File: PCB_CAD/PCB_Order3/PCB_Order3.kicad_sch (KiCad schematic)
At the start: 84 parts, among them SW1 SLW-883935-2A-D

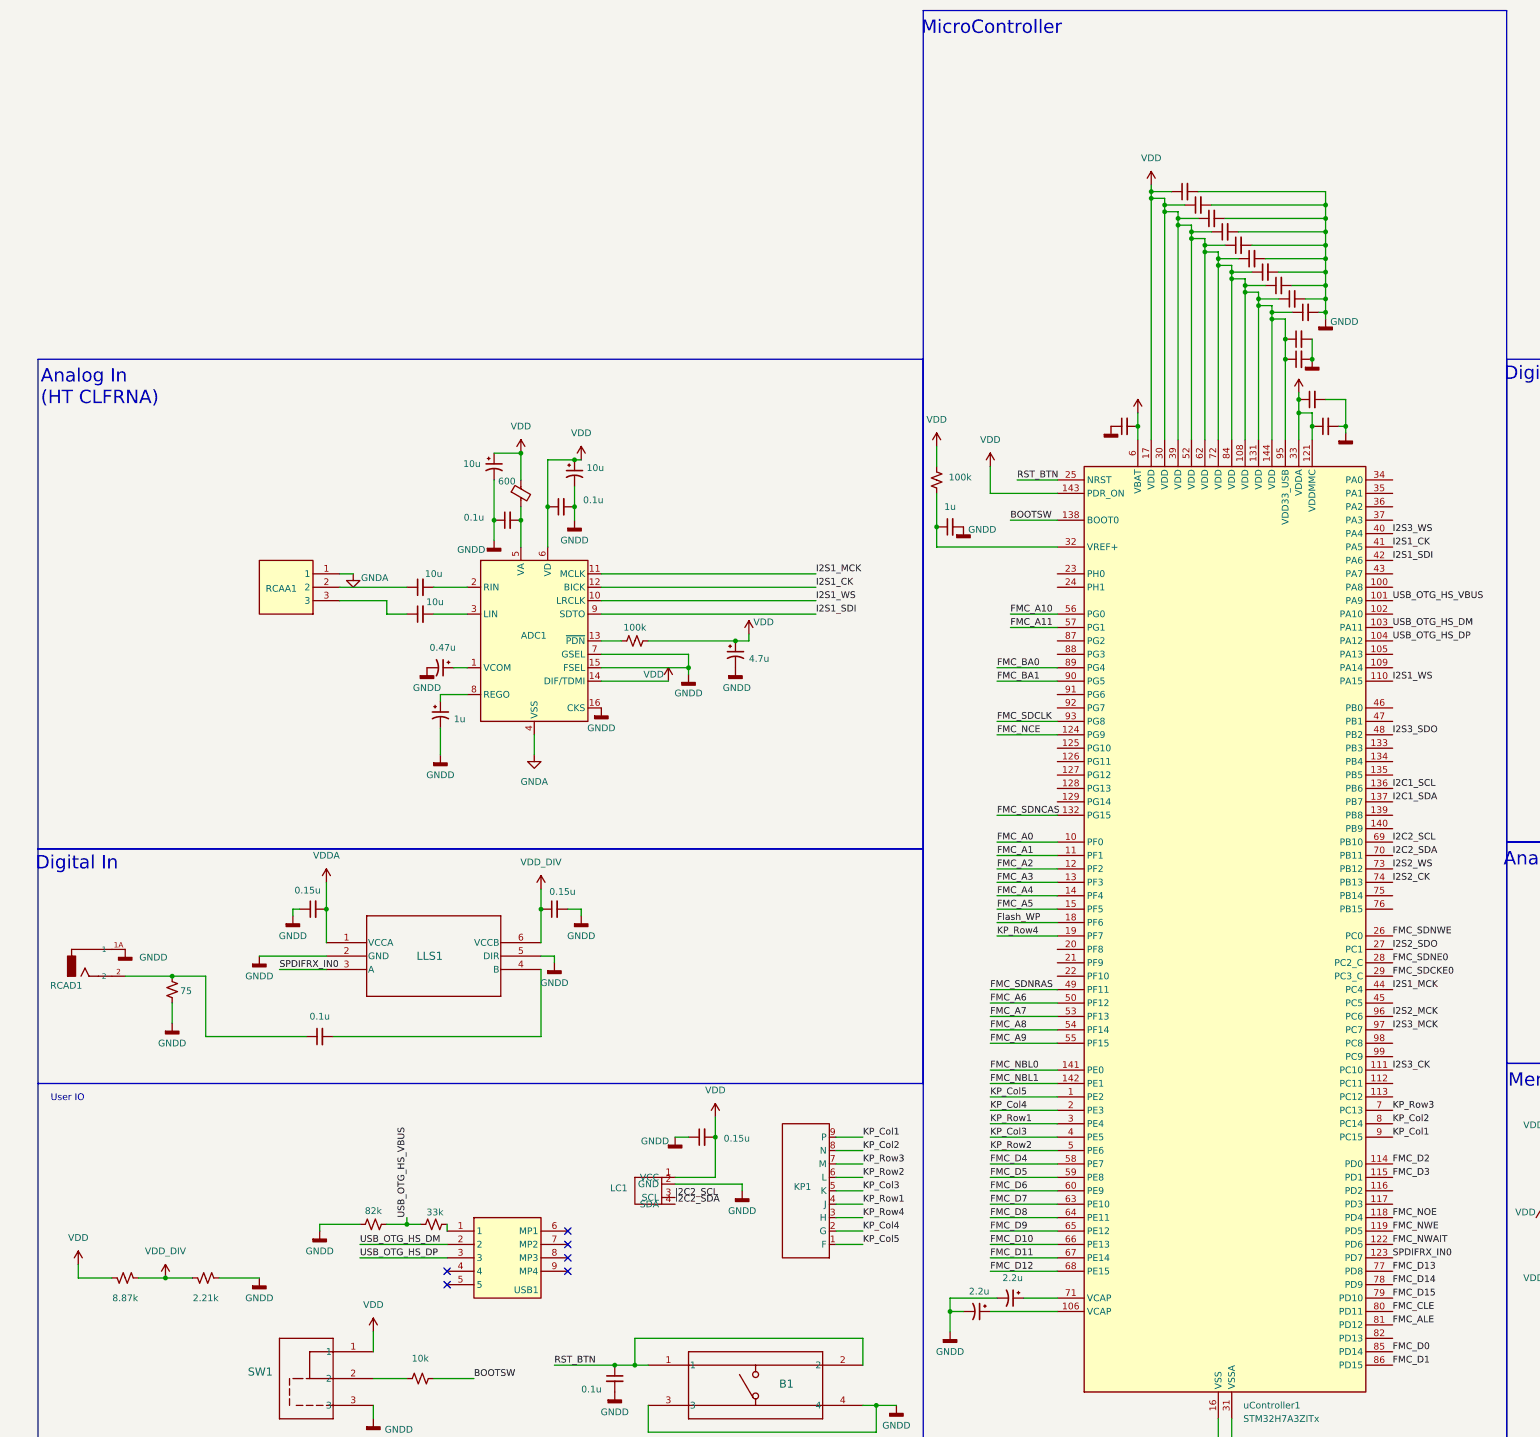
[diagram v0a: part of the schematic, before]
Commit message: minor fix microcontroller FMC
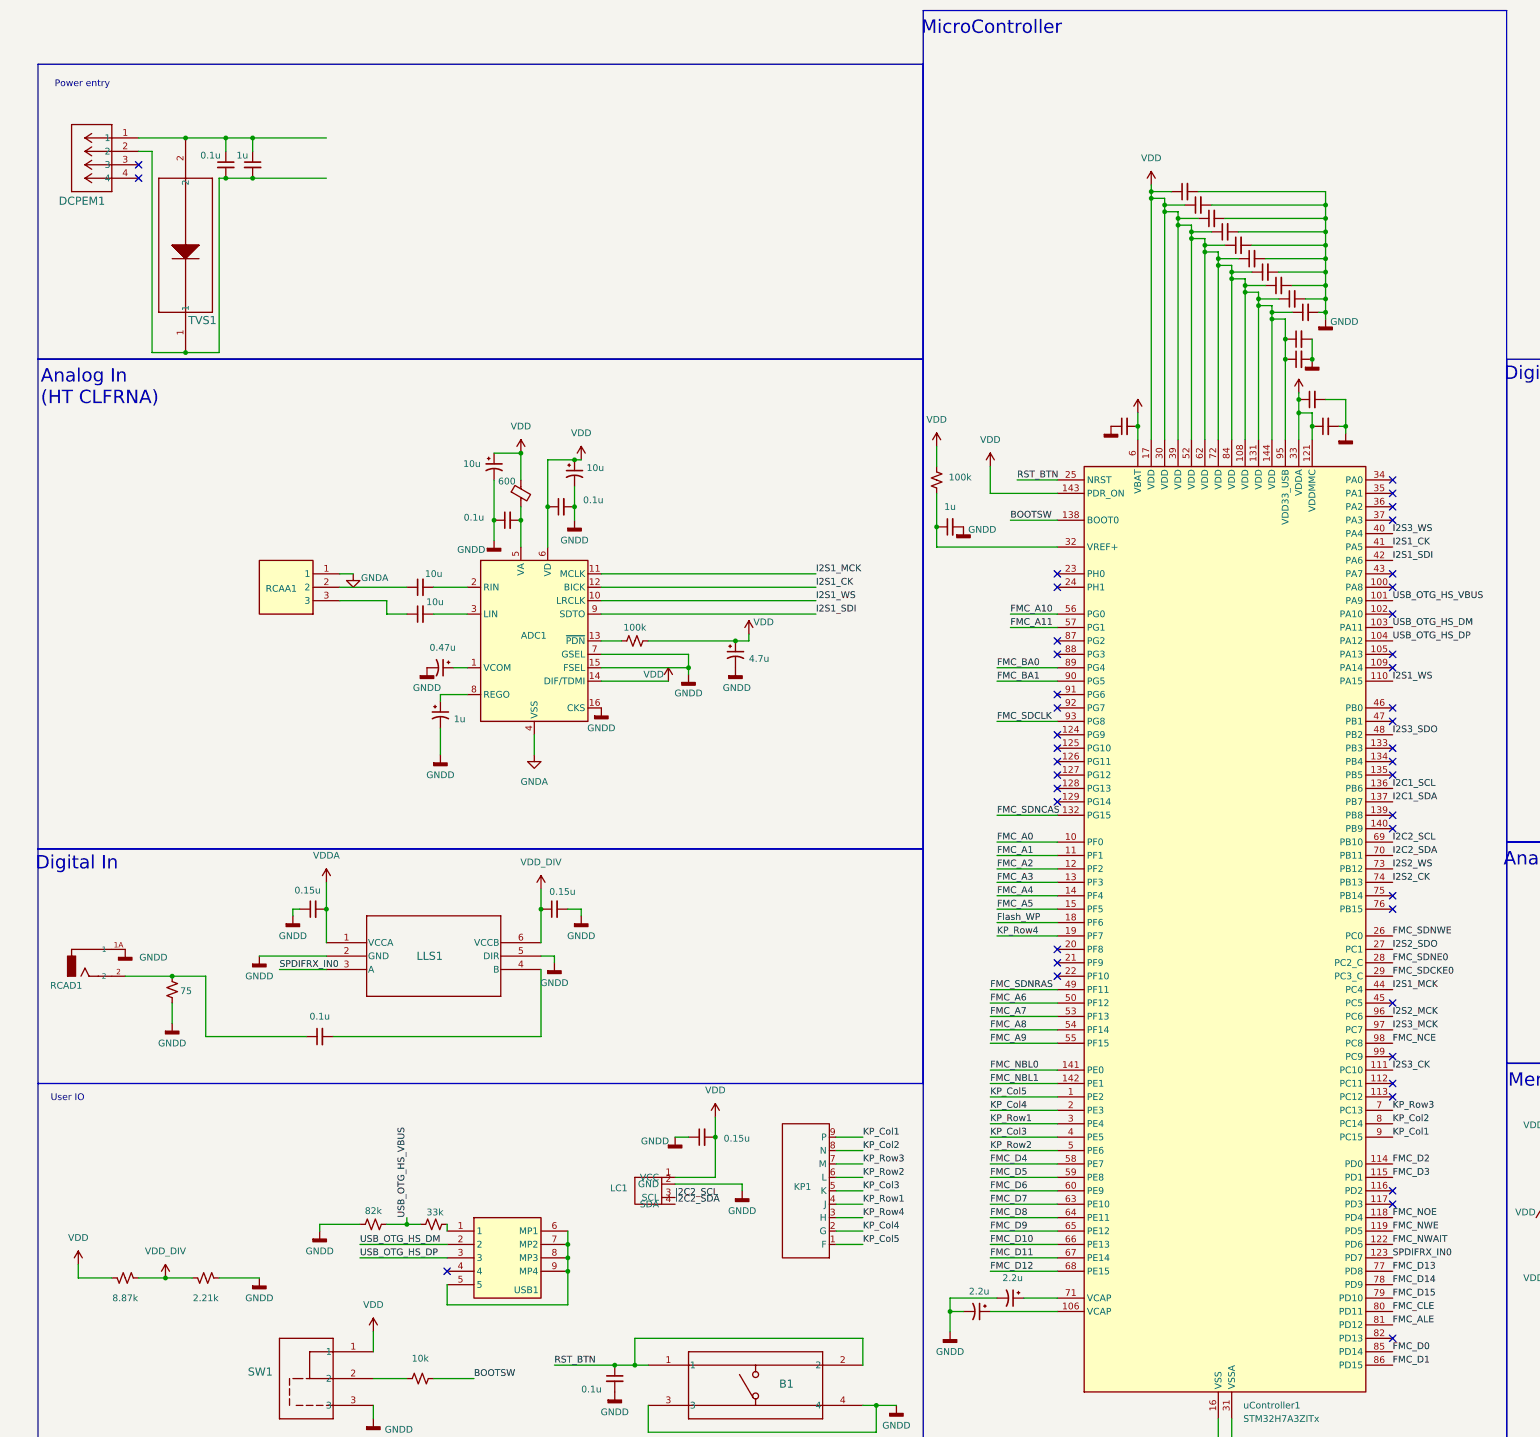
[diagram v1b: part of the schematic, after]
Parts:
- added DCPEM1: 470531000, CustomModels:CONN_SD-47053-001_H10p00_MOL, symbol 47053:470531000
- added PEC1: 0.1u, Capacitor_SMD:C_0805_2012Metric_Pad1.18x1.45mm_HandSolder, symbol Device:C_Small
- added PEC2: 1u, Capacitor_SMD:C_0805_2012Metric_Pad1.18x1.45mm_HandSolder, symbol Device:C_Small
- added TVS1: DF2S5M4SL_L3F, CustomModels:SOD-962 SL2_TOS, symbol TVS diode:DF2S5M4SL_L3F
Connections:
- net FMC_NCE: now also uController1.98 (PC8); no longer uController1.124 (PG9)
- net at USB1.5: now also USB1.6 (MP1), USB1.7 (MP2), USB1.8 (MP3), USB1.9 (MP4)
- new net: DCPEM1.1, PEC1.1, PEC2.1, TVS1.2
- new net: DCPEM1.2, PEC1.2, PEC2.2, TVS1.1
- no-connect marks 69 -> 106
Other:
- note added: "Power entry"

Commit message: change i2s configuration
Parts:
- added MbC1: 4.7u, Capacitor_SMD:C_0805_2012Metric_Pad1.18x1.45mm_HandSolder, symbol Device:C_Polarized_Small_US
- added PEC3: 47u, Capacitor_SMD:C_0805_2012Metric_Pad1.18x1.45mm_HandSolder, symbol Device:C_Polarized_Small_US
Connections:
- net GNDD: now also DCPEM1.1, PEC1.1, PEC2.1, TVS1.2, MbC1.2, PEC3.2
- net I2S2_CK: now also SPDIFTX1.8 (MPIO_C1)
- net I2S2_MCK: now also SPDIFTX1.7 (MPIO_C0)
- net I2S2_SDO: now also SPDIFTX1.10 (MPIO_C3)
- net I2S2_WS: now also SPDIFTX1.9 (MPIO_C2)
- net VDD: now also DCPEM1.2, PEC1.2, PEC2.2, TVS1.1, MbC1.1, PEC3.1
- net I2S3_CK: no longer names the net of uController1.111 (PC10)
- net I2S3_CK: no longer SPDIFTX1.8 (MPIO_C1)
- net I2S3_MCK: no longer names the net of uController1.97 (PC7)
- net I2S3_MCK: no longer SPDIFTX1.7 (MPIO_C0)
- net I2S3_SDO: no longer names the net of uController1.48 (PB2)
- net I2S3_SDO: no longer SPDIFTX1.10 (MPIO_C3)
- net I2S3_WS: no longer names the net of uController1.40 (PA4)
- net I2S3_WS: no longer SPDIFTX1.9 (MPIO_C2)
- no-connect marks 106 -> 110

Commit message: schematic power entry, schematic and cubeMX SW debug
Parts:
- added SWD1: Conn_01x02_Socket, Connector_PinSocket_2.54mm:PinSocket_1x02_P2.54mm_Vertical, symbol Connector:Conn_01x02_Socket
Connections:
- net DEBUG_SWDIO: now reaches uController1.105 (PA13)
- net DEBUG_SWDIO: now also SWD1.1 (Pin_1)
- net DEBUG_SWCLK: now reaches uController1.109 (PA14)
- net DEBUG_SWCLK: now also SWD1.2 (Pin_2)
- no-connect marks 110 -> 108
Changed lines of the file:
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@@
 	)
 	(no_connect
-		(at 462.28 208.28)
-	)
-	(no_connect
 		(at 610.87 360.68)
 	)
@@
 	)
 	(no_connect
-		(at 462.28 205.74)
-	)
-	(no_connect
 		(at 643.89 304.8)
 	)
@@
 	(wire
 		(pts
+			(xy 218.44 302.26) (xy 232.41 302.26)
+		)
+		(stroke
+			(width 0)
+			(type default)
+		)
+	)
+	(wire
+		(pts
 			(xy 567.69 300.99) (xy 556.26 300.99)
 		)
@@
 	(wire
 		(pts
+			(xy 218.44 304.8) (xy 232.41 304.8)
+		)
+		(stroke
+			(width 0)
+			(type default)
+		)
+	)
+	(wire
+		(pts
 			(xy 378.46 327.66) (xy 378.46 330.2)
 		)
@@
 		)
 	)
+	(label "DEBUG_SWDIO"
+		(at 462.28 205.74 0)
+		(fields_autoplaced yes)
+		(effects
+			(font
+				(size 1.27 1.27)
+			)
+			(justify left bottom)
+		)
+	)
 	(label "FMC_D6"
 		(at 386.08 307.34 0)
@@
 		)
 	)
+	(label "DEBUG_SWDIO"
+		(at 218.44 302.26 0)
+		(fields_autoplaced yes)
+		(effects
+			(font
+				(size 1.27 1.27)
+			)
+			(justify left bottom)
+		)
+	)
 	(label "FMC_NBL1"
 		(at 510.54 331.47 0)
@@
 		)
 	)
+	(label "DEBUG_SWCLK"
+		(at 462.28 208.28 0)
+		(fields_autoplaced yes)
+		(effects
+			(font
+				(size 1.27 1.27)
+			)
+			(justify left bottom)
+		)
+	)
 	(label "I2C2_SCL"
 		(at 326.39 308.61 0)
@@
 		)
 	)
+	(label "DEBUG_SWCLK"
+		(at 218.44 304.8 0)
+		(fields_autoplaced yes)
+		(effects
+			(font
+				(size 1.27 1.27)
+			)
+			(justify left bottom)
+		)
+	)
 	(label "FMC_A11"
 		(at 556.26 344.17 0)
@@
 					(unit 1)
 				)
+			)
+		)
+	)
+	(symbol
+		(lib_id "Connector:Conn_01x02_Socket")
+		(at 237.49 302.26 0)
+		(unit 1)
+		(exclude_from_sim no)
+		(in_bom yes)
+		(on_board yes)
+		(dnp no)
+		(fields_autoplaced yes)
+		(property "Reference" "SWD1"
+			(at 238.76 302.2599 0)
+			(effects
+				(font
+					(size 1.27 1.27)
+				)
+				(justify left)
+			)
+		)
+		(property "Value" "Conn_01x02_Socket"
+			(at 238.76 304.7999 0)
+			(effects
+				(font
+					(size 1.27 1.27)
+				)
+				(justify left)
+				(hide yes)
+			)
+		)
+		(property "Footprint" "Connector_PinSocket_2.54mm:PinSocket_1x02_P2.54mm_Vertical"
+			(at 237.49 302.26 0)
+			(effects
+				(font
+					(size 1.27 1.27)
+				)
+				(hide yes)
+			)
+		)
+		(property "Datasheet" "~"
+			(at 237.49 302.26 0)
+			(effects
+				(font
+					(size 1.27 1.27)
+				)
+				(hide yes)
+			)
+		)
+		(property "Description" "Generic connector, single row, 01x02, script generated"
+			(at 237.49 302.26 0)
+			(effects
+				(font
+					(size 1.27 1.27)
+				)
+				(hide yes)
+			)
+		)
+		(pin "2"
+		)
+		(pin "1"
+		)
+		(instances
+			(project ""
+				(path "/85a2a93a-53e0-46c8-b7f5-ee661b6f3053"
+					(reference "SWD1")
+					(unit 1)
+				)

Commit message: pinned out 3 sides of the microcontroller
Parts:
- removed SWD1: Conn_01x02_Socket, Connector_PinSocket_2.54mm:PinSocket_1x02_P2.54mm_Vertical, symbol Connector:Conn_01x02_Socket
- added J1: Conn_01x03_Socket, Connector_PinSocket_2.54mm:PinSocket_1x03_P2.54mm_Vertical_SMD_Pin1Right, symbol Connector:Conn_01x03_Socket
- BC1, MunC1, MunC2: footprint (none) -> Capacitor_SMD:C_0805_2012Metric_Pad1.18x1.45mm_HandSolder
- DB1, MR1, SR1, UR1, UR2: footprint (none) -> Resistor_SMD:R_0603_1608Metric_Pad0.98x0.95mm_HandSolder
- renumbered RCAA1 to RCAAin1, RCAA2 to RCAAout1, RCAD1 to RCADin1, RCAD2 to RCADout1
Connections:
- net DEBUG_SWCLK: now also J1.2 (Pin_2)
- net DEBUG_SWDIO: now also J1.1 (Pin_1)
- net GNDD: now also J1.3 (Pin_3)
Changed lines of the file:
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@@
 	)
 	(junction
+		(at 218.4627 307.34)
+		(diameter 0)
+		(color 0 0 0 0)
+	)
+	(junction
 		(at 449.58 128.27)
 		(diameter 0)
@@
 	(wire
 		(pts
+			(xy 218.4627 307.34) (xy 232.41 307.34)
+		)
+		(stroke
+			(width 0)
+			(type default)
+		)
+	)
+	(wire
+		(pts
 			(xy 440.69 133.35) (xy 449.58 133.35)
 		)
@@
 	(wire
 		(pts
+			(xy 218.44 307.34) (xy 218.4627 307.34)
+		)
+		(stroke
+			(width 0)
+			(type default)
+		)
+	)
+	(wire
+		(pts
 			(xy 227.33 148.59) (xy 233.68 148.59)
 		)
@@
 		(on_board yes)
 		(dnp no)
-		(property "Reference" "RCAA2"
+		(property "Reference" "RCAAout1"
 			(at 672.592 252.476 0)
 			(effects
@@
 			(project "PCB_Order2"
 				(path "/85a2a93a-53e0-46c8-b7f5-ee661b6f3053"
-					(reference "RCAA2")
+					(reference "RCAAout1")
 					(unit 1)
 				)
@@
 			)
 		)
-		(property "Footprint" ""
+		(property "Footprint" "Resistor_SMD:R_0603_1608Metric_Pad0.98x0.95mm_HandSolder"
 			(at 375.92 172.72 0)
 			(effects
@@
 		(on_board yes)
 		(dnp no)
-		(property "Reference" "RCAD1"
+		(property "Reference" "RCADin1"
 			(at 211.074 268.478 0)
 			(effects
@@
 			(project ""
 				(path "/85a2a93a-53e0-46c8-b7f5-ee661b6f3053"
-					(reference "RCAD1")
+					(reference "RCADin1")
 					(unit 1)
 				)
@@
 	)
 	(symbol
+		(lib_id "power:GNDD")
+		(at 218.4627 307.34 0)
+		(unit 1)
+		(exclude_from_sim no)
+		(in_bom yes)
+		(on_board yes)
+		(dnp no)
+		(fields_autoplaced yes)
+		(property "Reference" "#PWR0104"
+			(at 218.4627 313.69 0)
+			(effects
+				(font
+					(size 1.27 1.27)
+				)
+				(hide yes)
+			)
+		)
+		(property "Value" "GNDD"
+			(at 218.4627 311.15 0)
+			(effects
+				(font
+					(size 1.27 1.27)
+				)
+			)
+		)
+		(property "Footprint" ""
+			(at 218.4627 307.34 0)
+			(effects
+				(font
+					(size 1.27 1.27)
+				)
+				(hide yes)
+			)
+		)
+		(property "Datasheet" ""
+			(at 218.4627 307.34 0)
+			(effects
+				(font
+					(size 1.27 1.27)
+				)
+				(hide yes)
+			)
+		)
+		(property "Description" "Power symbol creates a global label with name \"GNDD\" , digital ground"
+			(at 218.4627 307.34 0)
+			(effects
+				(font
+					(size 1.27 1.27)
+				)
+				(hide yes)
+			)
+		)
+		(pin "1"
+		)
+		(instances
+			(project "PCB_Order3"
+				(path "/85a2a93a-53e0-46c8-b7f5-ee661b6f3053"
+					(reference "#PWR0104")
+					(unit 1)
+				)
+			)
+		)
+	)
+	(symbol
 		(lib_id "power:VDD")
 		(at 297.18 167.64 0)
@@
 	)
 	(symbol
+		(lib_id "Connector:Conn_01x03_Socket")
+		(at 237.49 304.8 0)
+		(unit 1)
+		(exclude_from_sim no)
+		(in_bom yes)
+		(on_board yes)
+		(dnp no)
+		(fields_autoplaced yes)
+		(property "Reference" "J1"
+			(at 238.76 303.5299 0)
+			(effects
+				(font
+					(size 1.27 1.27)
+				)
+				(justify left)
+			)
+		)
+		(property "Value" "Conn_01x03_Socket"
+			(at 238.76 306.0699 0)
+			(effects
+				(font
+					(size 1.27 1.27)
+				)
+				(justify left)
+			)
+		)
+		(property "Footprint" "Connector_PinSocket_2.54mm:PinSocket_1x03_P2.54mm_Vertical_SMD_Pin1Right"
+			(at 237.49 304.8 0)
+			(effects
+				(font
+					(size 1.27 1.27)
+				)
+				(hide yes)
+			)
+		)
+		(property "Datasheet" "~"
+			(at 237.49 304.8 0)
+			(effects
+				(font
+					(size 1.27 1.27)
+				)
+				(hide yes)
+			)
+		)
+		(property "Description" "Generic connector, single row, 01x03, script generated"
+			(at 237.49 304.8 0)
+			(effects
+				(font
+					(size 1.27 1.27)
+				)
+				(hide yes)
+			)
+		)
+		(pin "3"
+		)
+		(pin "1"
+		)
+		(pin "2"
+		)
+		(instances
+			(project ""
+				(path "/85a2a93a-53e0-46c8-b7f5-ee661b6f3053"
+					(reference "J1")
+					(unit 1)
+				)
+			)
+		)
+	)
+	(symbol
 		(lib_id "custom:GME12864")
 		(at 321.31 307.34 0)
@@
 		(on_board yes)
 		(dnp no)
-		(property "Reference" "RCAD2"
+		(property "Reference" "RCADout1"
 			(at 741.426 202.946 0)
 			(effects
@@
 			(project ""
 				(path "/85a2a93a-53e0-46c8-b7f5-ee661b6f3053"
-					(reference "RCAD2")
+					(reference "RCADout1")
 					(unit 1)
 				)
@@
 			)
 		)
-		(property "Footprint" ""
+		(property "Footprint" "Capacitor_SMD:C_0805_2012Metric_Pad1.18x1.45mm_HandSolder"
 			(at 444.5 146.05 0)
 			(effects
@@
 		(on_board yes)
 		(dnp no)
-		(property "Reference" "RCAA1"
+		(property "Reference" "RCAAin1"
 			(at 254.762 193.294 0)
 			(effects
@@
 			(project ""
 				(path "/85a2a93a-53e0-46c8-b7f5-ee661b6f3053"
-					(reference "RCAA1")
+					(reference "RCAAin1")
 					(unit 1)
 				)
@@
 			)
 		)
-		(property "Footprint" ""
+		(property "Footprint" "Resistor_SMD:R_0603_1608Metric_Pad0.98x0.95mm_HandSolder"
 			(at 278.13 342.9 0)
 			(effects
@@
 			)
 		)
-		(property "Footprint" ""
+		(property "Footprint" "Capacitor_SMD:C_0805_2012Metric_Pad1.18x1.45mm_HandSolder"
 			(at 444.5 149.86 0)
 			(effects
@@
 			)
 		)
-		(property "Footprint" ""
+		(property "Footprint" "Capacitor_SMD:C_0805_2012Metric_Pad1.18x1.45mm_HandSolder"
 			(at 314.96 342.9 0)
 			(effects
@@
 	)
 	(symbol
-		(lib_id "Connector:Conn_01x02_Socket")
-		(at 237.49 302.26 0)
-		(unit 1)
-		(exclude_from_sim no)
-		(in_bom yes)
-		(on_board yes)
-		(dnp no)
-		(fields_autoplaced yes)
-		(property "Reference" "SWD1"
-			(at 238.76 302.2599 0)
-			(effects
-				(font
-					(size 1.27 1.27)
-				)
-				(justify left)
-			)
-		)
-		(property "Value" "Conn_01x02_Socket"
-			(at 238.76 304.7999 0)
-			(effects
-				(font
-					(size 1.27 1.27)
-				)
-				(justify left)
-				(hide yes)
-			)
-		)
-		(property "Footprint" "Connector_PinSocket_2.54mm:PinSocket_1x02_P2.54mm_Vertical"
-			(at 237.49 302.26 0)
-			(effects
-				(font
-					(size 1.27 1.27)
-				)
-				(hide yes)
-			)
-		)
-		(property "Datasheet" "~"
-			(at 237.49 302.26 0)
-			(effects
-				(font
-					(size 1.27 1.27)
-				)
-				(hide yes)
-			)
-		)
-		(property "Description" "Generic connector, single row, 01x02, script generated"
-			(at 237.49 302.26 0)
-			(effects
-				(font
-					(size 1.27 1.27)
-				)
-				(hide yes)
-			)
-		)
-		(pin "2"
-		)
-		(pin "1"
-		)
-		(instances
-			(project ""
-				(path "/85a2a93a-53e0-46c8-b7f5-ee661b6f3053"
-					(reference "SWD1")
-					(unit 1)
-				)
-			)
-		)
-	)
-	(symbol
 		(lib_id "Device:R_Small_US")
 		(at 280.67 313.69 90)
@@
 			)
 		)
-		(property "Footprint" ""
+		(property "Footprint" "Resistor_SMD:R_0603_1608Metric_Pad0.98x0.95mm_HandSolder"
 			(at 280.67 313.69 0)
 			(effects
@@
 			)
 		)
-		(property "Footprint" ""
+		(property "Footprint" "Resistor_SMD:R_0603_1608Metric_Pad0.98x0.95mm_HandSolder"
 			(at 269.24 313.69 0)
 			(effects
@@
 			)
 		)
-		(property "Footprint" ""
+		(property "Footprint" "Resistor_SMD:R_0603_1608Metric_Pad0.98x0.95mm_HandSolder"
 			(at 512.572 248.92 90)
 			(effects

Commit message: power daughterboard final review, some main schematic small fixes
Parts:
- added DXnC2, DXnC3: 0.1u, Capacitor_SMD:C_0805_2012Metric_Pad1.18x1.45mm_HandSolder, symbol Device:C_Small
- DXnC1, LLSOC1, LLSOC2: value 0.15u -> 0.1u
- TVS: renamed from TVS1; footprint CustomModels:SOD-962 SL2_TOS -> Diode_SMD:D_0201_0603Metric_Pad0.64x0.40mm_HandSolder
- renumbered DCPEM1 to DCPEM, LLS1 to LLSIN, LLS2 to LLSOUT, RCAAin1 to RCAAin, SPDIFTX1 to SPDIFTX
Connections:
- net GNDD: now also SPDIFTX.38 (GNDRX), SPDIFTX.41 (AGND), DXnC2.2, DXnC3.1
- net VDD: now also SPDIFTX.36 (VDDRX), SPDIFTX.42 (VCC), DXnC2.1, DXnC3.2
- no-connect marks 108 -> 104
